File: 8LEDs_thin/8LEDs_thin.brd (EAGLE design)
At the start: 23.8 x 30.5 mm, 10 parts

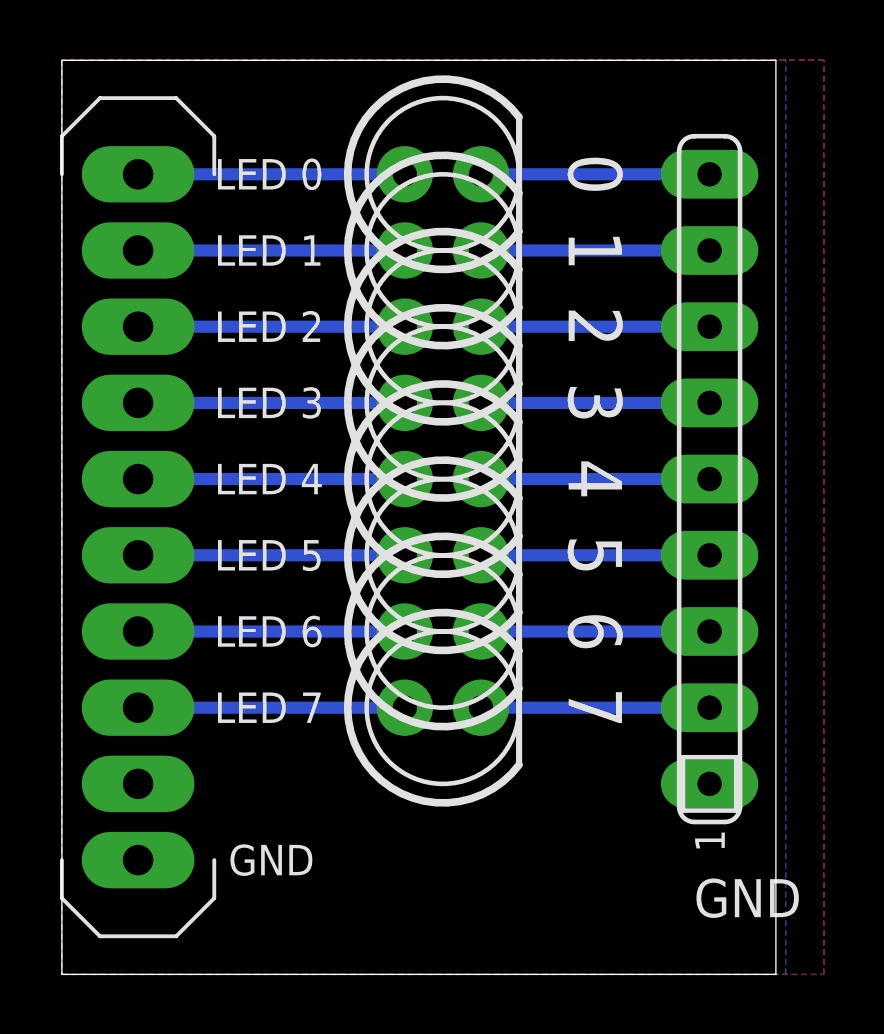
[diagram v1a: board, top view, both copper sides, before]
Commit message: added inliner, more top text
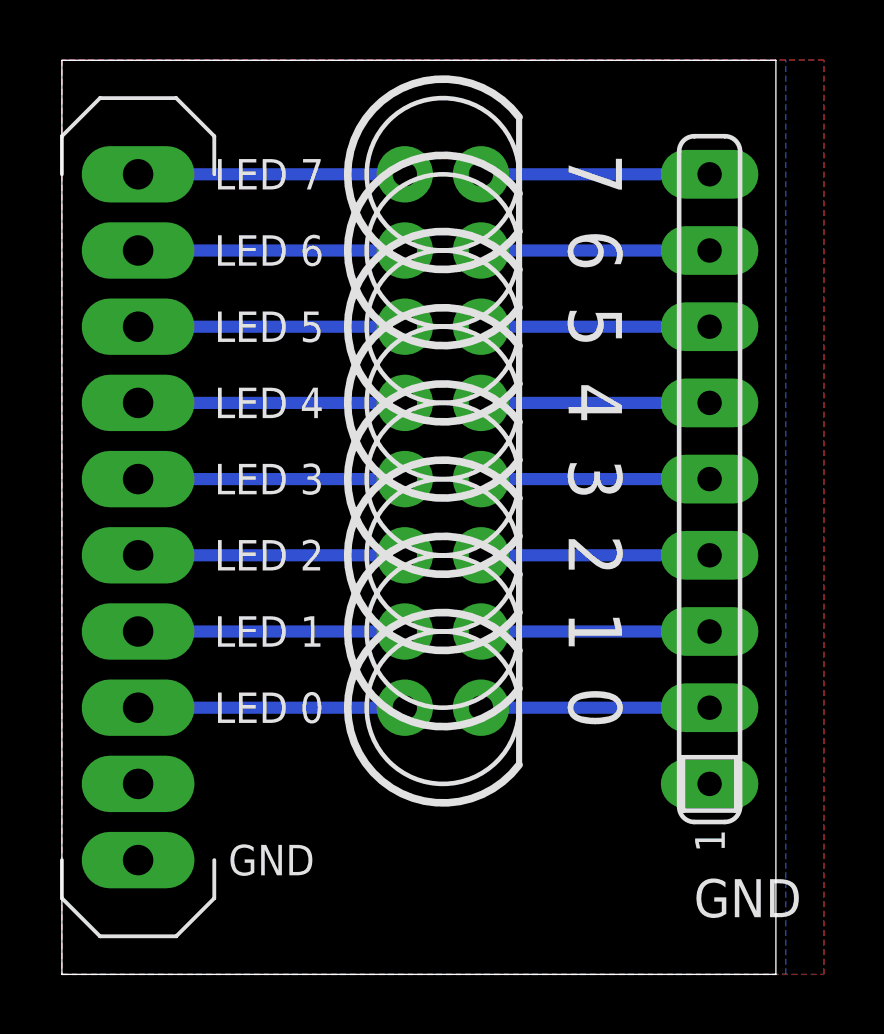
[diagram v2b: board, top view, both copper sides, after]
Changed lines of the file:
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@@
 <text x="65.405" y="35.56" size="1.016" layer="25" align="center">GND</text>
 <text x="81.28" y="34.29" size="1.27" layer="25" align="center">GND</text>
-<text x="63.5" y="48.26" size="1.016" layer="25" align="center-left">LED 4</text>
-<text x="63.5" y="50.8" size="1.016" layer="25" align="center-left">LED 3</text>
-<text x="63.5" y="53.34" size="1.016" layer="25" align="center-left">LED 2</text>
-<text x="63.5" y="55.88" size="1.016" layer="25" align="center-left">LED 1</text>
-<text x="63.5" y="58.42" size="1.016" layer="25" align="center-left">LED 0</text>
-<text x="63.5" y="45.72" size="1.016" layer="25" align="center-left">LED 5</text>
-<text x="63.5" y="43.18" size="1.016" layer="25" align="center-left">LED 6</text>
-<text x="63.5" y="40.64" size="1.016" layer="25" align="center-left">LED 7</text>
-<text x="76.2" y="58.42" size="1.778" layer="25" rot="SR270" align="center">0</text>
-<text x="76.2" y="55.88" size="1.778" layer="25" rot="SR270" align="center">1</text>
-<text x="76.2" y="53.34" size="1.778" layer="25" rot="SR270" align="center">2</text>
-<text x="76.2" y="50.8" size="1.778" layer="25" rot="SR270" align="center">3</text>
-<text x="76.2" y="48.26" size="1.778" layer="25" rot="SR270" align="center">4</text>
-<text x="76.2" y="45.72" size="1.778" layer="25" rot="SR270" align="center">5</text>
-<text x="76.2" y="43.18" size="1.778" layer="25" rot="SR270" align="center">6</text>
-<text x="76.2" y="40.64" size="1.778" layer="25" rot="SR270" align="center">7</text>
+<text x="63.5" y="48.26" size="1.016" layer="25" align="center-left">LED 3</text>
+<text x="63.5" y="50.8" size="1.016" layer="25" align="center-left">LED 4</text>
+<text x="63.5" y="53.34" size="1.016" layer="25" align="center-left">LED 5</text>
+<text x="63.5" y="55.88" size="1.016" layer="25" align="center-left">LED 6</text>
+<text x="63.5" y="58.42" size="1.016" layer="25" align="center-left">LED 7</text>
+<text x="63.5" y="45.72" size="1.016" layer="25" align="center-left">LED 2</text>
+<text x="63.5" y="43.18" size="1.016" layer="25" align="center-left">LED 1</text>
+<text x="63.5" y="40.64" size="1.016" layer="25" align="center-left">LED 0</text>
+<text x="76.2" y="58.42" size="1.778" layer="25" rot="SR270" align="center">7</text>
+<text x="76.2" y="55.88" size="1.778" layer="25" rot="SR270" align="center">6</text>
+<text x="76.2" y="53.34" size="1.778" layer="25" rot="SR270" align="center">5</text>
+<text x="76.2" y="50.8" size="1.778" layer="25" rot="SR270" align="center">4</text>
+<text x="76.2" y="48.26" size="1.778" layer="25" rot="SR270" align="center">3</text>
+<text x="76.2" y="45.72" size="1.778" layer="25" rot="SR270" align="center">2</text>
+<text x="76.2" y="43.18" size="1.778" layer="25" rot="SR270" align="center">1</text>
+<text x="76.2" y="40.64" size="1.778" layer="25" rot="SR270" align="center">0</text>
 </plain>
 <attributes>
